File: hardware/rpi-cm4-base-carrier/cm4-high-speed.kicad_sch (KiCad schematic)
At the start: 5 parts

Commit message: Finished schematic
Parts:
- gave numbers to parts that had none: 4
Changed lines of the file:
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@@
   (symbol (lib_id "power:GND") (at 40.64 175.26 0) (unit 1)
     (in_bom yes) (on_board yes)
-    (property "Reference" "#PWR?" (id 0) (at 40.64 181.61 0)
+    (property "Reference" "#PWR0111" (id 0) (at 40.64 181.61 0)
       (effects (font (size 1.27 1.27)) hide)
     )
@@
   (symbol (lib_id "power:GND") (at 106.68 175.26 0) (unit 1)
     (in_bom yes) (on_board yes)
-    (property "Reference" "#PWR?" (id 0) (at 106.68 181.61 0)
+    (property "Reference" "#PWR0112" (id 0) (at 106.68 181.61 0)
       (effects (font (size 1.27 1.27)) hide)
     )
@@
   (symbol (lib_id "power:GND") (at 153.67 63.5 0) (unit 1)
     (in_bom yes) (on_board yes)
-    (property "Reference" "#PWR?" (id 0) (at 153.67 69.85 0)
+    (property "Reference" "#PWR0113" (id 0) (at 153.67 69.85 0)
       (effects (font (size 1.27 1.27)) hide)
     )
@@
   (symbol (lib_id "power:GND") (at 195.58 71.12 0) (unit 1)
     (in_bom yes) (on_board yes)
-    (property "Reference" "#PWR?" (id 0) (at 195.58 77.47 0)
+    (property "Reference" "#PWR0115" (id 0) (at 195.58 77.47 0)
       (effects (font (size 1.27 1.27)) hide)
     )
@@
   (symbol (lib_id "power:GND") (at 227.33 66.04 0) (unit 1)
     (in_bom yes) (on_board yes)
-    (property "Reference" "#PWR?" (id 0) (at 227.33 72.39 0)
+    (property "Reference" "#PWR0114" (id 0) (at 227.33 72.39 0)
       (effects (font (size 1.27 1.27)) hide)
     )
@@
   (symbol (lib_id "Device:R") (at 195.58 52.07 0) (unit 1)
     (in_bom yes) (on_board yes)
-    (property "Reference" "R?" (id 0) (at 198.12 50.8 0)
+    (property "Reference" "R7" (id 0) (at 198.12 50.8 0)
       (effects (font (size 1.27 1.27)) (justify left))
     )
@@
   (symbol (lib_id "Device:R") (at 195.58 64.77 0) (unit 1)
     (in_bom yes) (on_board yes)
-    (property "Reference" "R?" (id 0) (at 198.12 63.5 0)
+    (property "Reference" "R8" (id 0) (at 198.12 63.5 0)
       (effects (font (size 1.27 1.27)) (justify left))
     )
@@
   (symbol (lib_id "Connector:USB_OTG") (at 227.33 50.8 0) (mirror y) (unit 1)
     (in_bom yes) (on_board yes)
-    (property "Reference" "J?" (id 0) (at 233.68 50.8 0)
+    (property "Reference" "J4" (id 0) (at 233.68 50.8 0)
       (effects (font (size 1.27 1.27)) (justify right))
     )
@@
   (symbol (lib_id "Power_Protection:TPD2EUSB30") (at 153.67 50.8 0) (unit 1)
     (in_bom yes) (on_board yes)
-    (property "Reference" "U?" (id 0) (at 153.67 40.64 0))
+    (property "Reference" "U2" (id 0) (at 153.67 40.64 0))
     (property "Value" "TPD2EUSB30" (id 1) (at 153.67 43.18 0))
     (property "Footprint" "Package_TO_SOT_SMD:Texas_DRT-3" (id 2) (at 134.62 58.42 0)

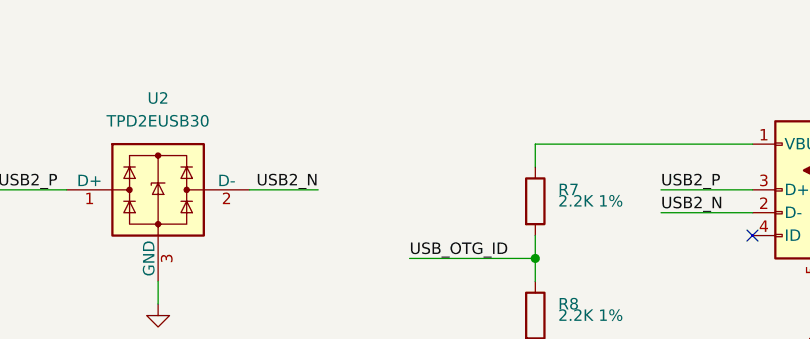
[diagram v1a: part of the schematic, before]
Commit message: Added labels to schematic sections
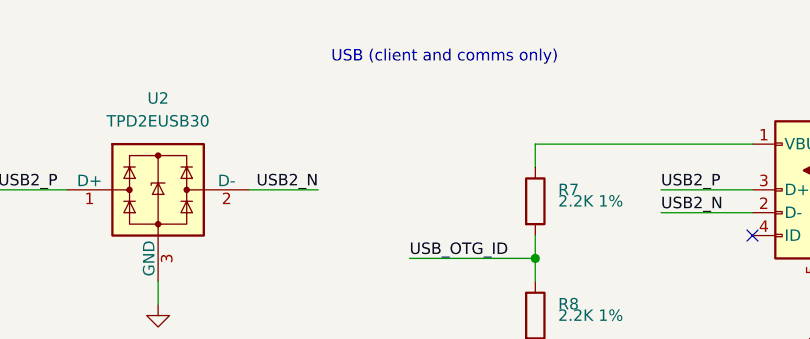
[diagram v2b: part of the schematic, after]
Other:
- note added: "USB (client and comms only)"
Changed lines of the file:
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@@
     (stroke (width 0) (type solid) (color 0 0 0 0))
+  )
+  (text "USB (client and comms only)" (at 198.12 36.83 180)
+    (effects (font (size 1.27 1.27)) (justify right bottom))
   )
   (label "USB_OTG_ID" (at 119.38 45.72 180)
